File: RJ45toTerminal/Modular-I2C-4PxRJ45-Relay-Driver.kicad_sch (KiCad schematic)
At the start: 123 parts, among them J1 Conn_02x03_Odd_Even, J2 Conn_02x03_Odd_Even, J3 Screw_Terminal_01x02, J4 Screw_Terminal_01x02, Q51 2N7002, Q52 2N7002, Q53 2N7002, Q54 2N7002, Q55 2N7002, Q56 2N7002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

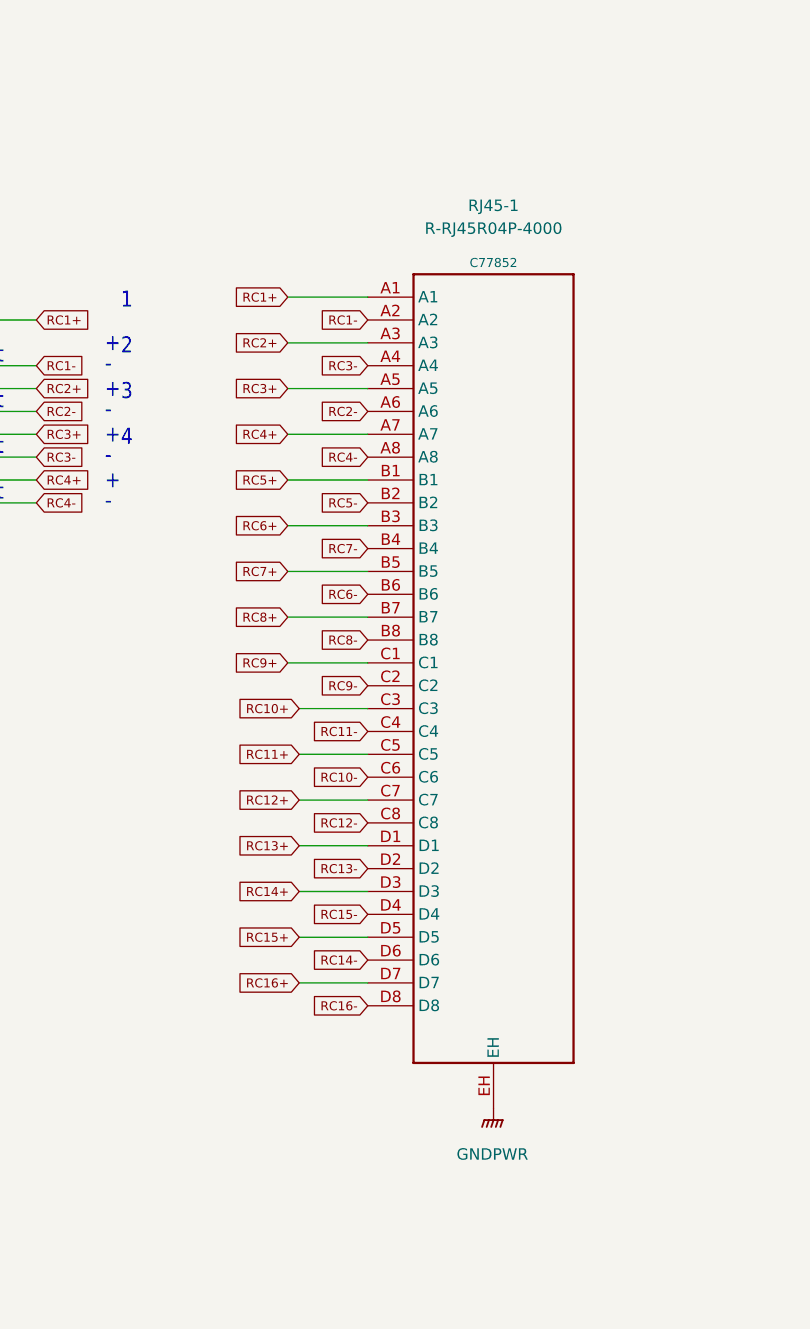
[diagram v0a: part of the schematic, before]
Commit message: RJ45 to Pluggable break out
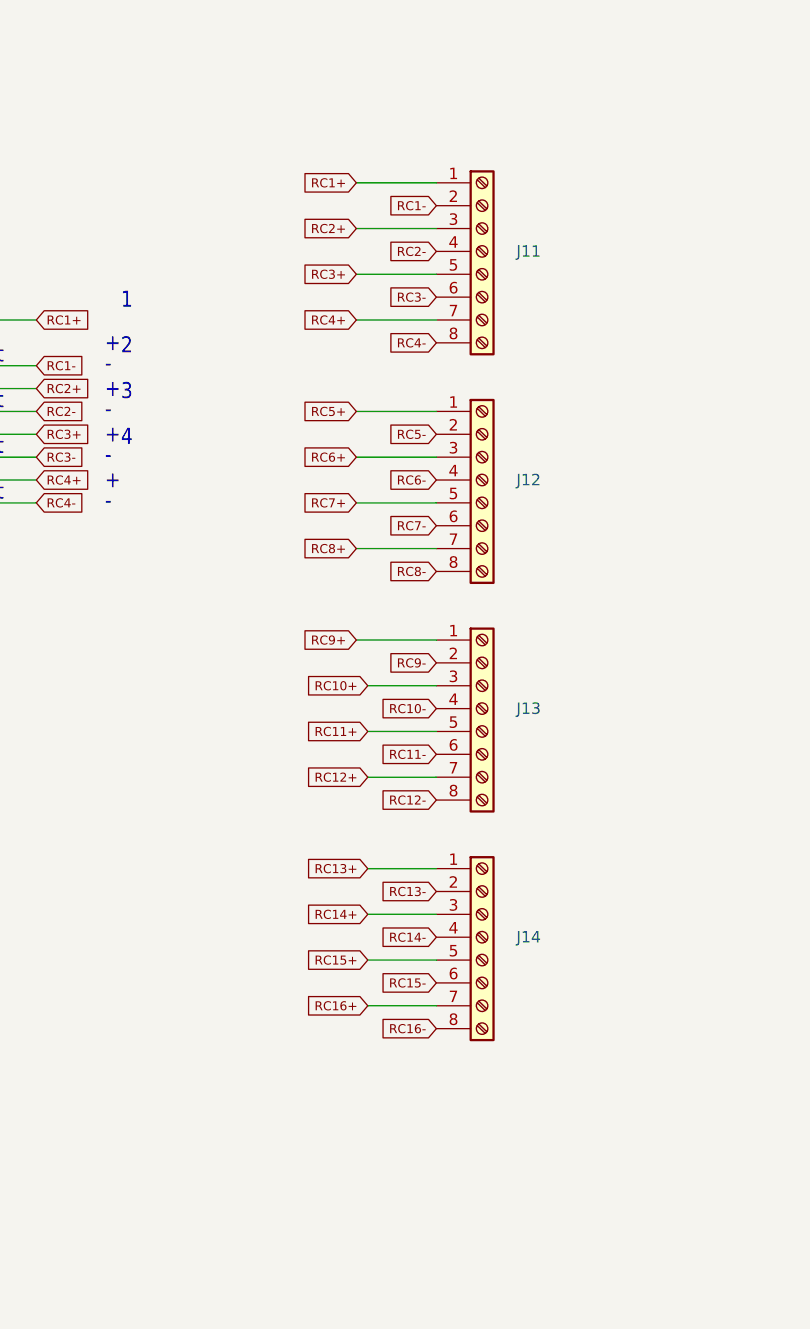
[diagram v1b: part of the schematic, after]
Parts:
- removed RJ45-1: R-RJ45R04P-4000, Vizista:CONN-TH_DS1129-02-S80BP, symbol ICMS-8S1:R-RJ45R08P-8000
- added J11, J12, J13, J14: Screw_Terminal_01x08, VizistaHA:CONN-TH_4P-P3.50_JILN_JL15EDGRHC-35004B02, symbol Connector:Screw_Terminal_01x08
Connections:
- net RC1+: now also J11.1 (Pin_1)
- net RC1-: now also J11.2 (Pin_2)
- net RC10+: now also J13.3 (Pin_3)
- net RC10-: now also J13.4 (Pin_4)
- net RC11+: now also J13.5 (Pin_5)
- net RC11-: now also J13.6 (Pin_6)
- net RC12+: now also J13.7 (Pin_7)
- net RC12-: now also J13.8 (Pin_8)
- net RC13+: now also J14.1 (Pin_1)
- net RC13-: now also J14.2 (Pin_2)
- net RC14+: now also J14.3 (Pin_3)
- net RC14-: now also J14.4 (Pin_4)
- net RC15+: now also J14.5 (Pin_5)
- net RC15-: now also J14.6 (Pin_6)
- net RC16+: now also J14.7 (Pin_7)
- net RC16-: now also J14.8 (Pin_8)
- net RC2+: now also J11.3 (Pin_3)
- net RC2-: now also J11.4 (Pin_4)
- net RC3+: now also J11.5 (Pin_5)
- net RC3-: now also J11.6 (Pin_6)
- net RC4+: now also J11.7 (Pin_7)
- net RC4-: now also J11.8 (Pin_8)
- net RC5+: now also J12.1 (Pin_1)
- net RC5-: now also J12.2 (Pin_2)
- net RC6+: now also J12.3 (Pin_3)
- net RC6-: now also J12.4 (Pin_4)
- net RC7+: now also J12.5 (Pin_5)
- net RC7-: now also J12.6 (Pin_6)
- net RC8+: now also J12.7 (Pin_7)
- net RC8-: now also J12.8 (Pin_8)
- net RC9+: now also J13.1 (Pin_1)
- net RC9-: now also J13.2 (Pin_2)
